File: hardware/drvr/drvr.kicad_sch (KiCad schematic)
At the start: 0 parts

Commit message: added current amps, basic PCB positions
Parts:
- added J101, J102, J103, J104, J105, J106: PinHeader2x2, mcrmv:PinHeader2x2_1mm_Solder, symbol Connector_Generic:Conn_02x02_Odd_Even
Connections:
- new net GH_P1_1: J104.2 (Pin_2)
- new net GH_P1_2: J104.4 (Pin_4)
- new net GH_P2_1: J105.2 (Pin_2)
- new net GH_P2_2: J105.4 (Pin_4)
- new net GH_P3_1: J106.2 (Pin_2)
- new net GH_P3_2: J106.4 (Pin_4)
- new net GL_P1_1: J101.3 (Pin_3)
- new net GL_P1_2: J101.1 (Pin_1)
- new net GL_P2_1: J102.3 (Pin_3)
- new net GL_P2_2: J102.1 (Pin_1)
- new net GL_P3_1: J103.3 (Pin_3)
- new net GL_P3_2: J103.1 (Pin_1)
- new net GND: J101.2 (Pin_2), J102.2 (Pin_2), J103.2 (Pin_2)
- new net NTC1: J101.4 (Pin_4)
- new net NTC2: J102.4 (Pin_4)
- new net NTC3: J103.4 (Pin_4)
- new net S1_N: J104.3 (Pin_3)
- new net S1_P: J104.1 (Pin_1)
- new net S2_N: J105.3 (Pin_3)
- new net S2_P: J105.1 (Pin_1)
- new net S3_N: J106.3 (Pin_3)
- new net S3_P: J106.1 (Pin_1)
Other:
- added sheet amp0 (amp.kicad_sch)
- added sheet amp1 (amp.kicad_sch)
- added sheet amp2 (amp.kicad_sch)
- company: (none) -> github.com/${AUTHOR}
- title: (none) -> ${TITLE} - ${SUBTITLE}

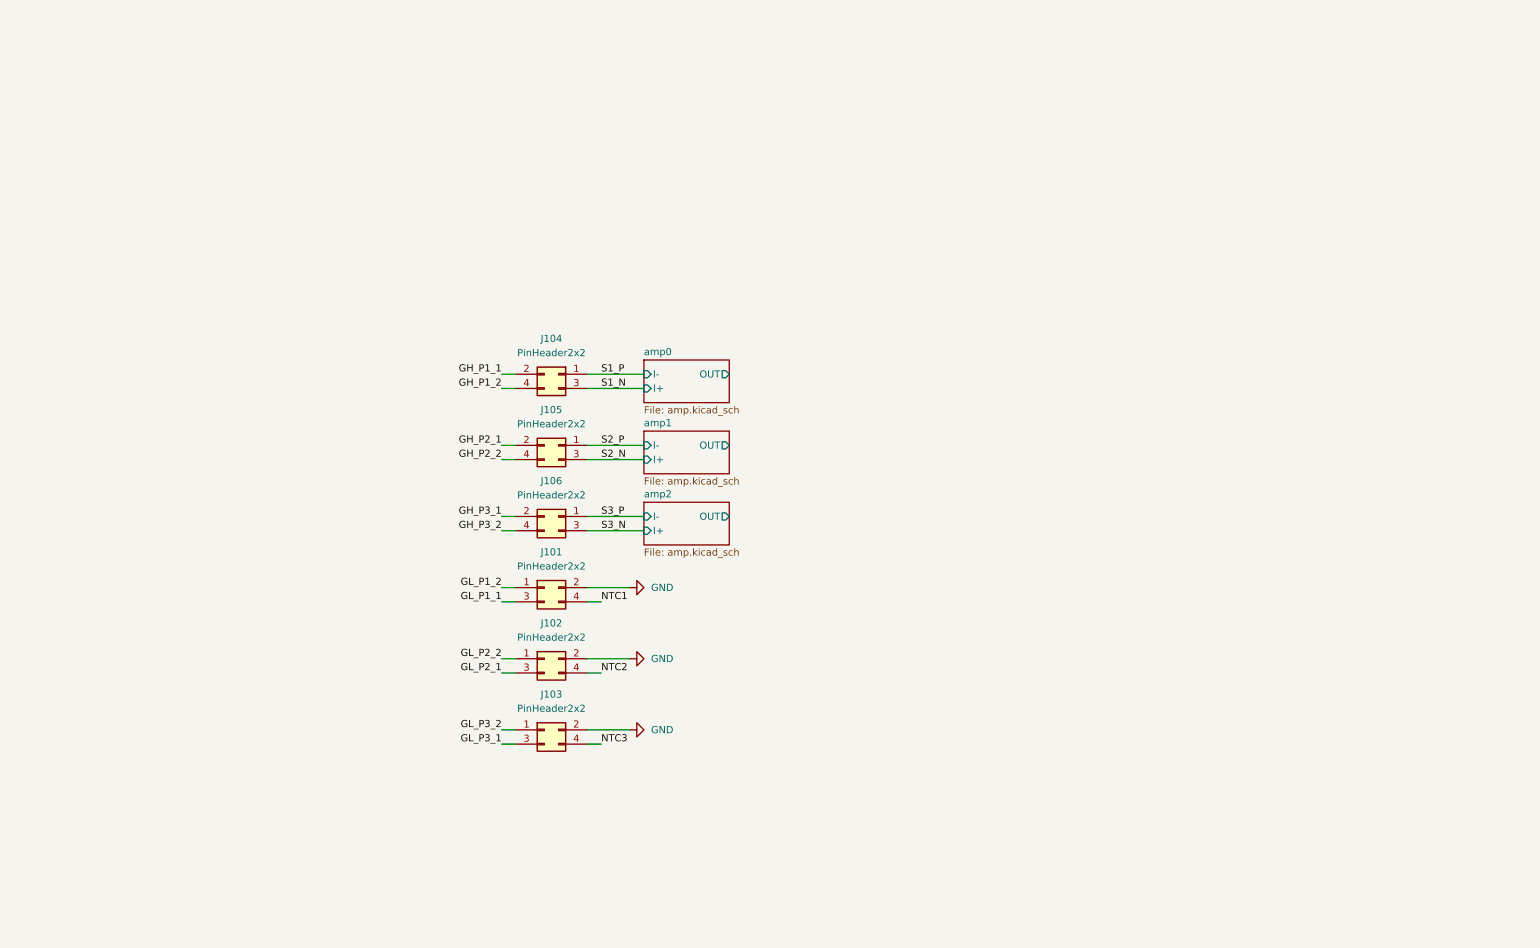
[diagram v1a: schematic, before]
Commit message: added solder targets, expanded project structure
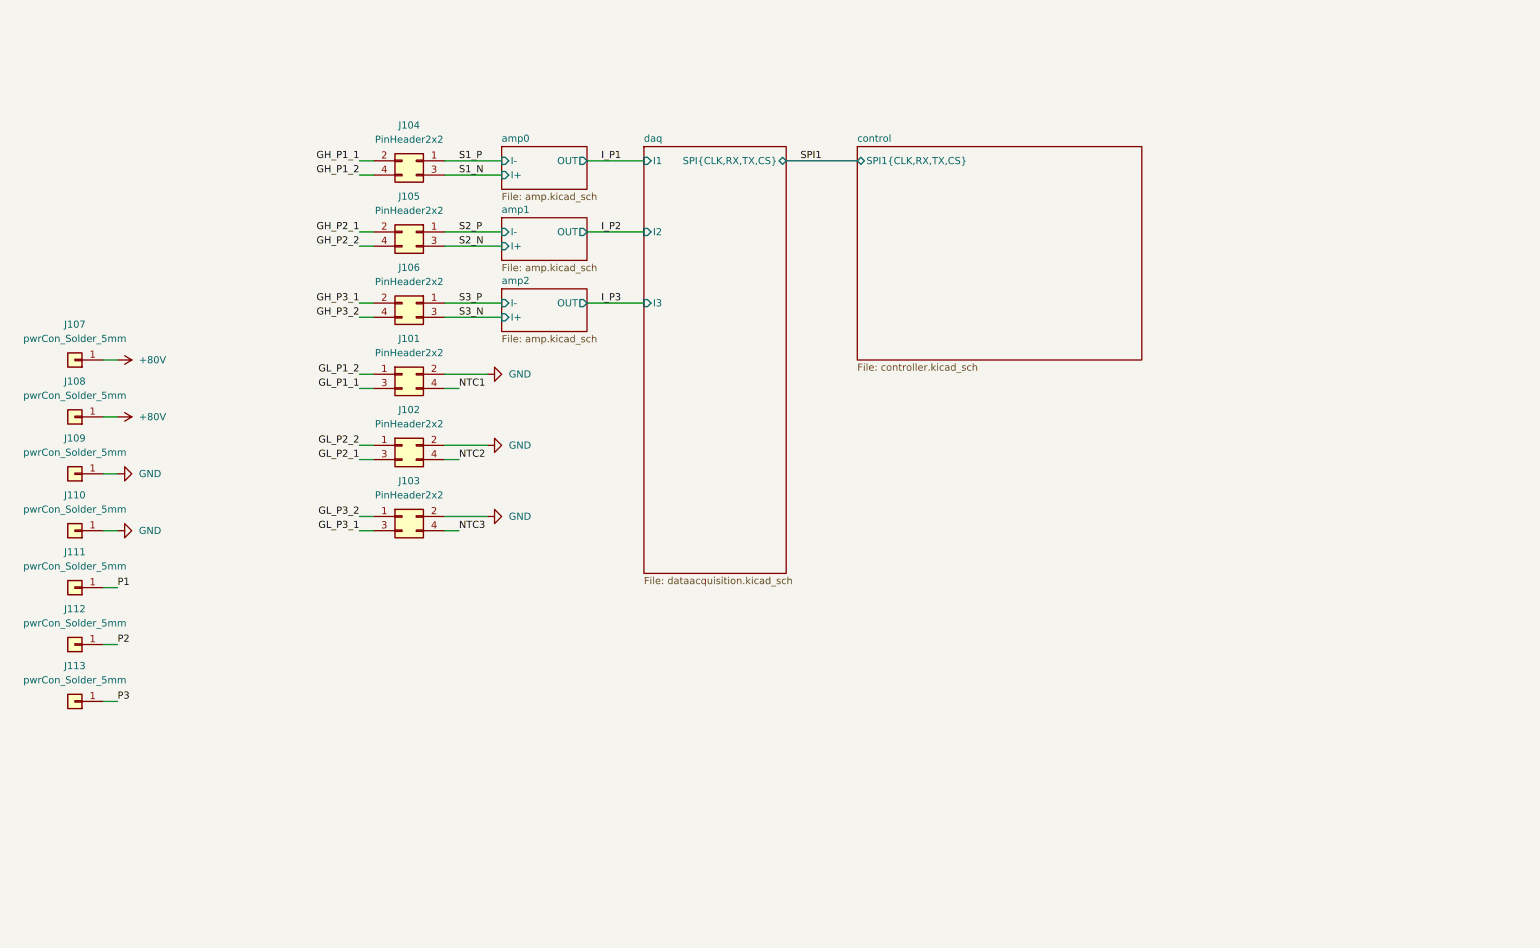
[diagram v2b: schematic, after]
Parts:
- added J107, J108, J109, J110, J111, J112, J113: pwrCon_Solder_5mm, mcrmv:0.1x5mm_Strip_Cutout, symbol Connector_Generic:Conn_01x01
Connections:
- net GND: now also J109.1 (Pin_1), J110.1 (Pin_1)
- new net +80V: J107.1 (Pin_1), J108.1 (Pin_1)
- new net P1: J111.1 (Pin_1)
- new net P2: J112.1 (Pin_1)
- new net P3: J113.1 (Pin_1)
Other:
- added sheet control (controller.kicad_sch)
- added sheet daq (dataacquisition.kicad_sch)
- moved on the sheet: J101, J102, J103, J104, J105, J106

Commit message: added initial gate-drive design
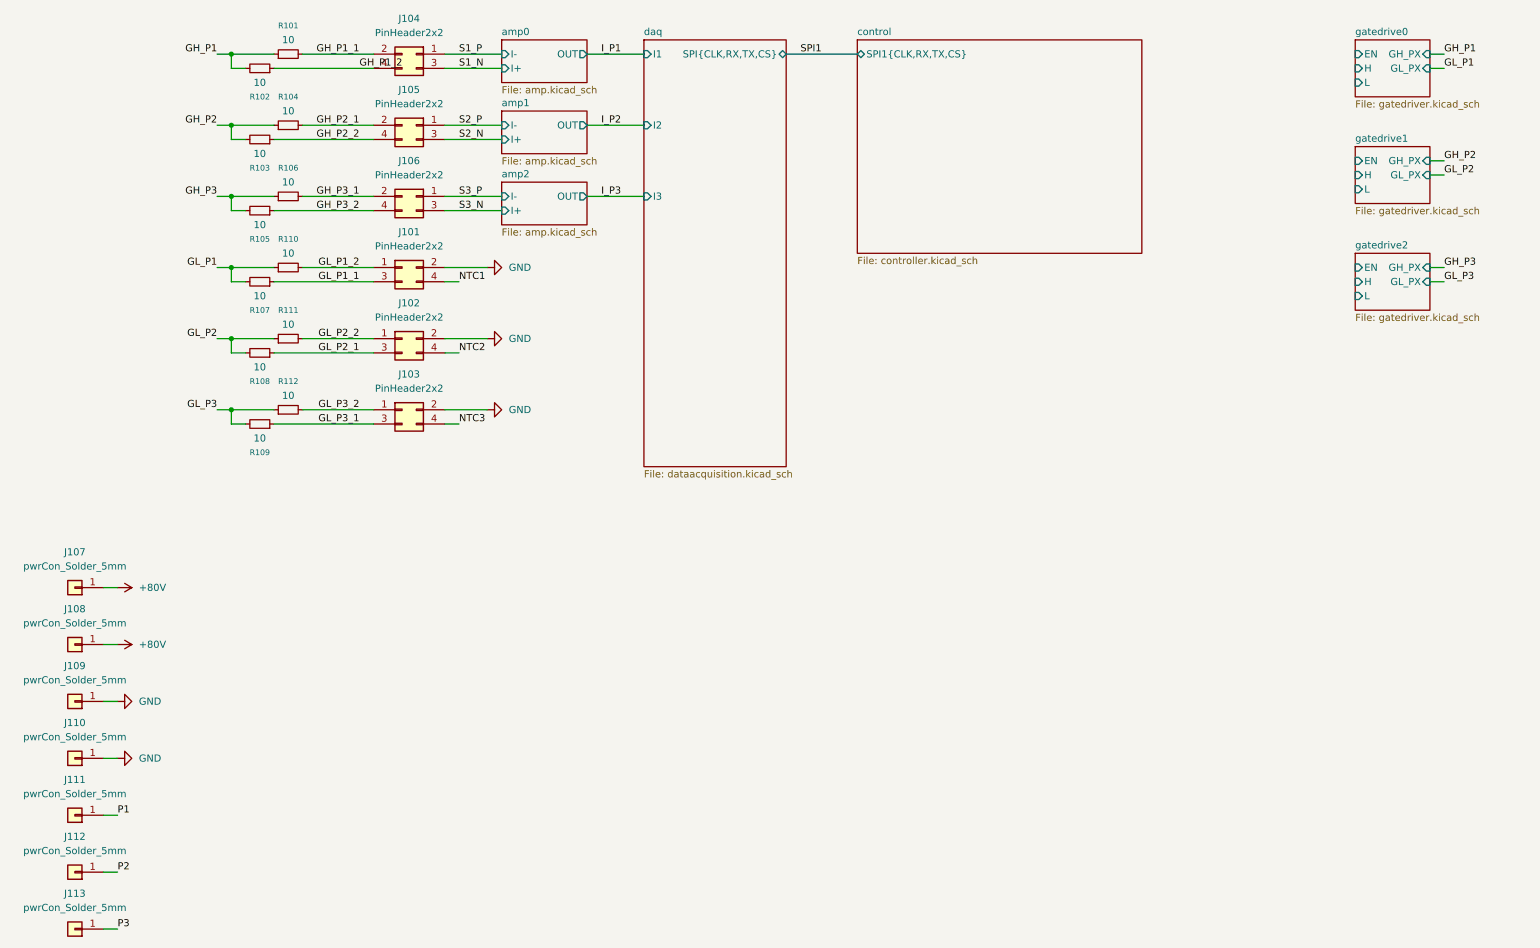
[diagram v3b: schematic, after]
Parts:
- added R101, R102, R103, R104, R105, R106, R107, R108, R109, R110, R111, R112: 10, Resistor_SMD:R_0402_1005Metric, symbol Device:R_Small
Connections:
- net GH_P1_1: now also R101.2
- net GH_P1_2: now also R102.1
- net GH_P2_1: now also R104.2
- net GH_P2_2: now also R103.1
- net GH_P3_1: now also R106.2
- net GH_P3_2: now also R105.1
- net GL_P1_1: now also R107.1
- net GL_P1_2: now also R110.2
- net GL_P2_1: now also R108.1
- net GL_P2_2: now also R111.2
- net GL_P3_1: now also R109.1
- net GL_P3_2: now also R112.2
- new net GH_P1: R101.1, R102.2
- new net GH_P2: R103.2, R104.1
- new net GH_P3: R105.2, R106.1
- new net GL_P1: R107.2, R110.1
- new net GL_P2: R108.2, R111.1
- new net GL_P3: R109.2, R112.1
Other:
- added sheet gatedrive0 (gatedriver.kicad_sch)
- added sheet gatedrive1 (gatedriver.kicad_sch)
- added sheet gatedrive2 (gatedriver.kicad_sch)
- moved on the sheet: J101, J102, J103, J104, J105, J106, J107, J108, J109, J110, J111, J112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
